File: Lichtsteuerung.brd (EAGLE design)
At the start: 157.7 x 86.4 mm, 173 parts, among them IC1 74HC595D, IC10 TSR_1-2450, IC11 MEGA64-A, IC12 75176AD, IC13 DS1307SO8, IC2 74HC595D, IC3 74HC595D, IC4 74HC595D, IC5 LM317LD, IC6 LM317LD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

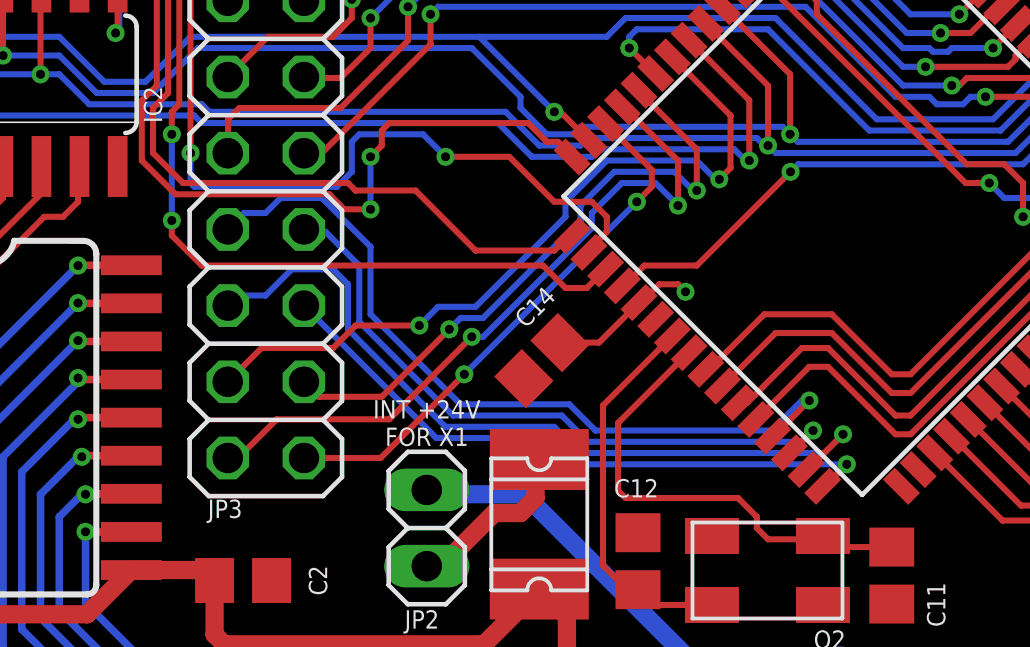
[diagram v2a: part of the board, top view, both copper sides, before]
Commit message: Added TVS Diode and 100n capacitor for the reset line
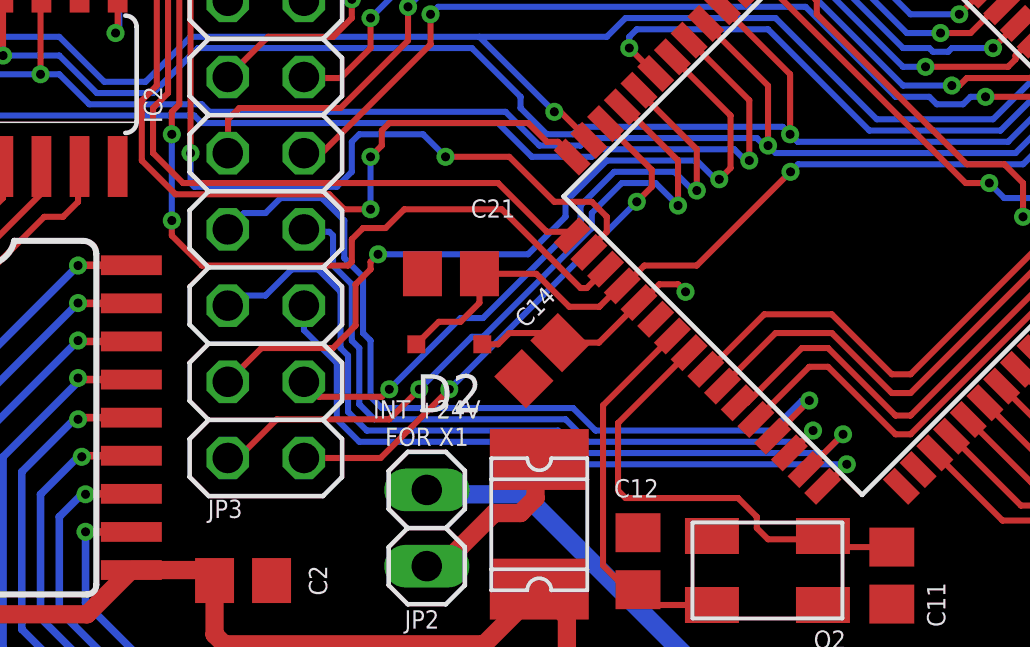
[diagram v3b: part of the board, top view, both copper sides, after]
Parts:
- added C21: 100n, rcl:C0805
- added D2: (no value), diode:SOD323-R
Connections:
- net +5V: now also D2.C
- net GND: now also C21.2
- net RESET: now also C21.1, D2.A
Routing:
- net RESET: track 111.5 -> 120.6 mm
- net +5V: track 121.9 -> 124.8 mm
- net LED4: track 40.1 -> 42.1 mm
- net AUXCON_10: track 22.3 -> 23.9 mm
- net AUXCON_9: track 26.5 -> 28.1 mm
- net AUXCON_12: track 21.4 -> 23.0 mm
- net AUXCON_11: track 26.4 -> 27.7 mm
- net AUXCON_13: track 25.0 -> 26.0 mm
